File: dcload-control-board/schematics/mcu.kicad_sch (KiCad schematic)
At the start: 38 parts, among them J200 Conn_01x06_Male, J201 Conn_01x04_Male, J202 Conn_01x04_Male, U200 STM32F411RCT6, Y200 25MHz

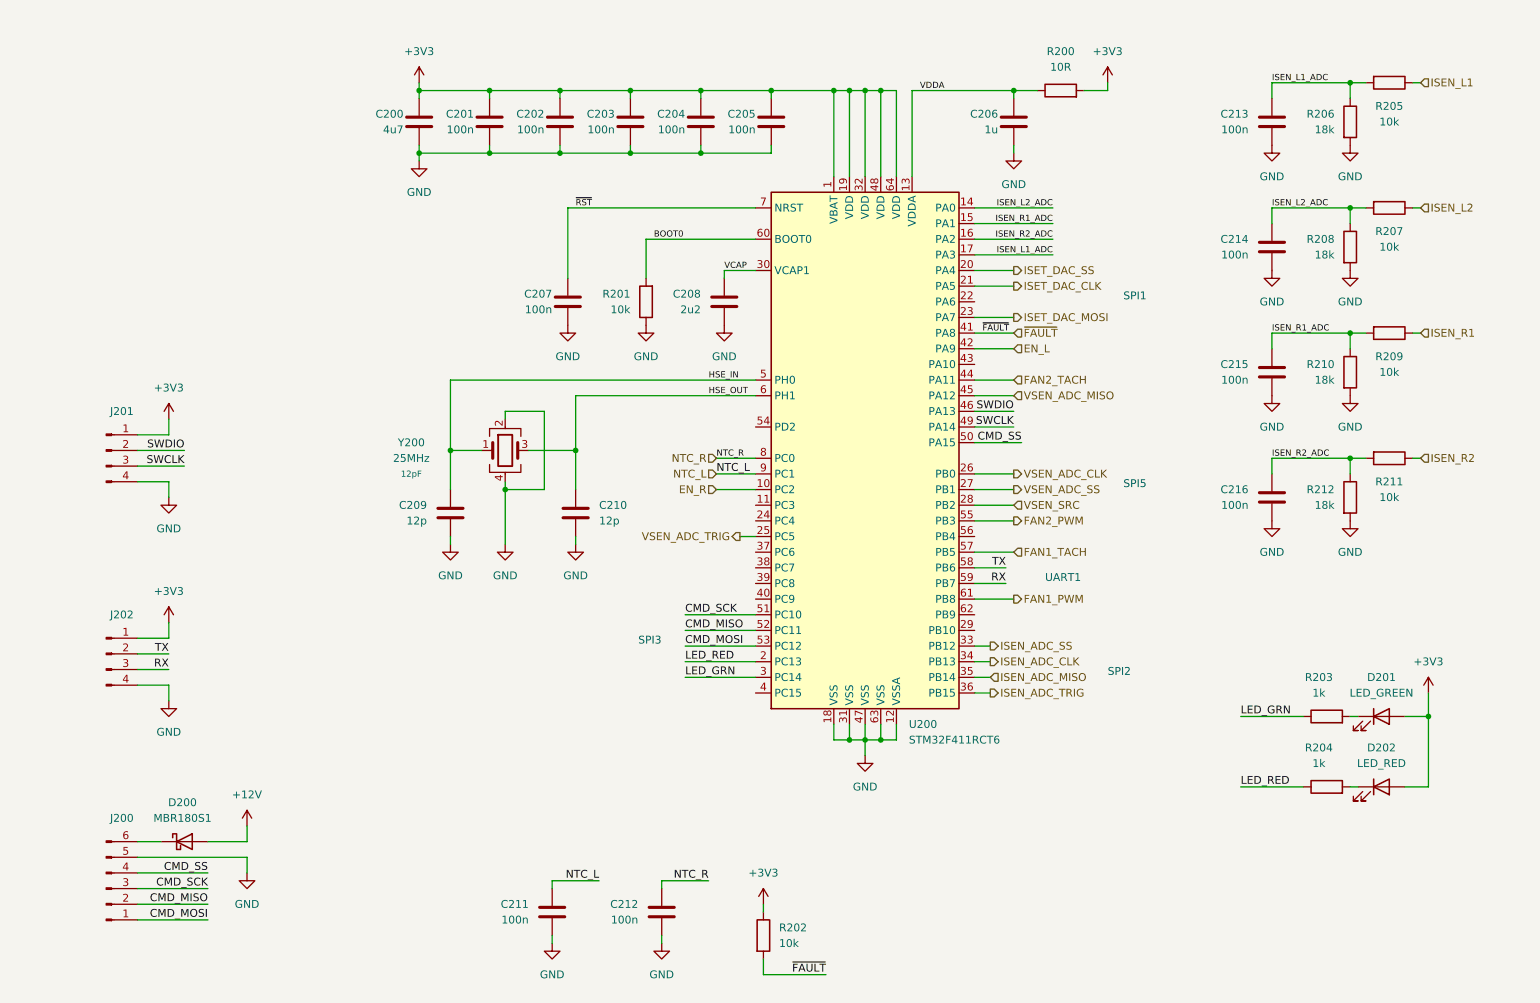
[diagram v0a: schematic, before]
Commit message: add: interface panel board
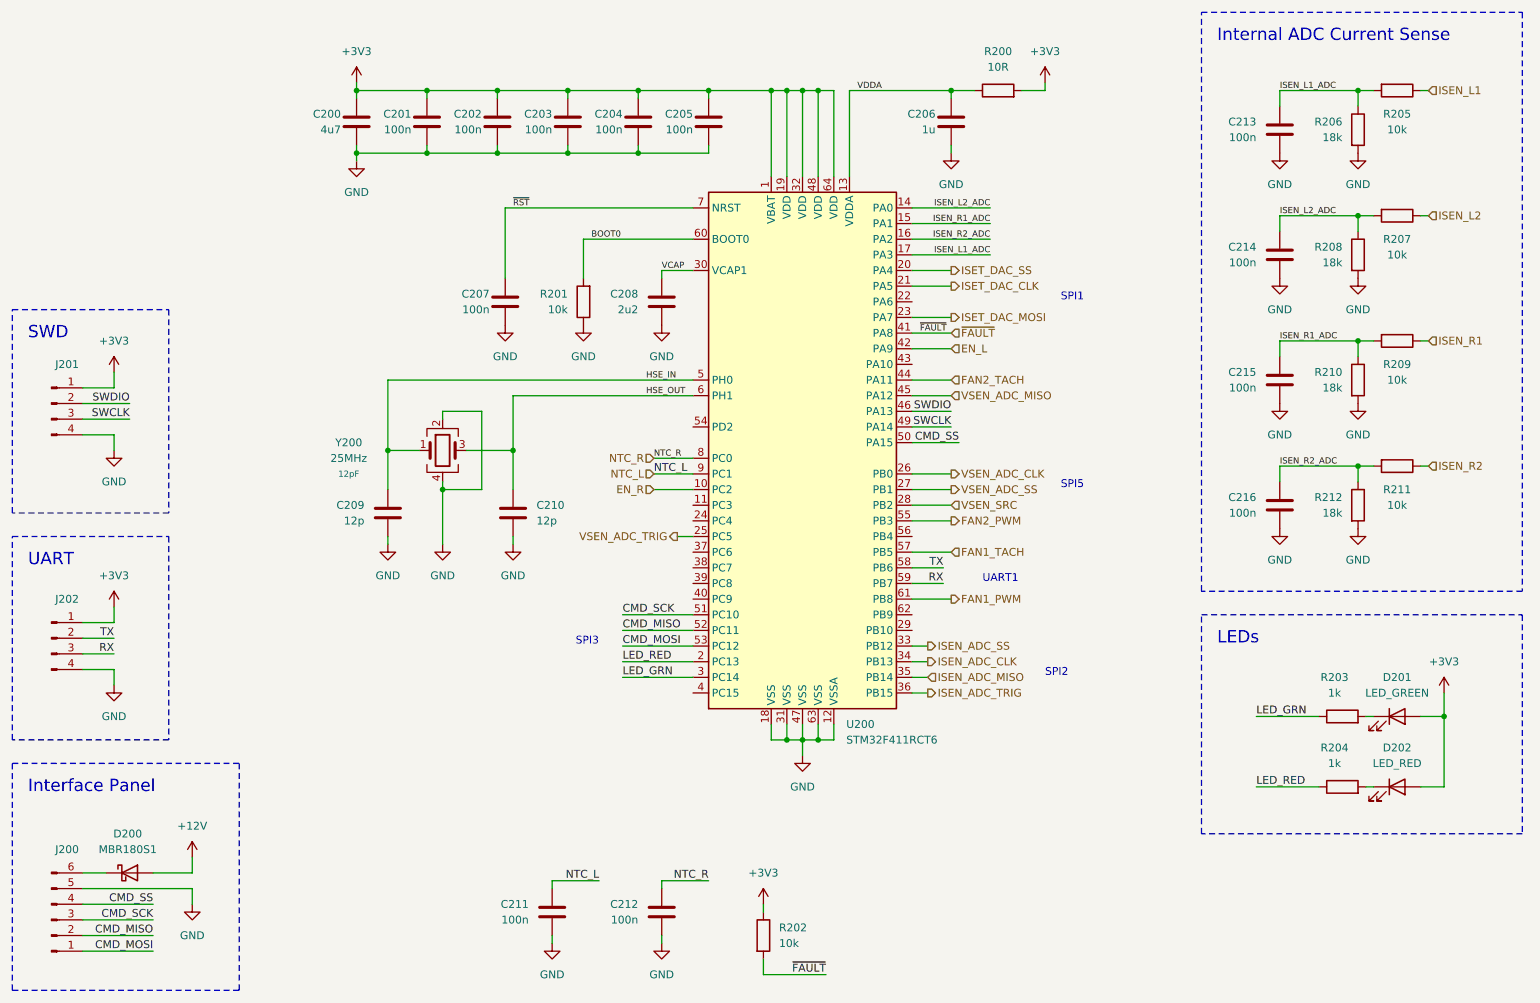
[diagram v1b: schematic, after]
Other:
- note added: "Interface Panel"
- note added: "Internal ADC Current Sense"
- note added: "LEDs"
- note added: "SWD"
- note added: "UART"
- moved on the sheet: C200, C201, C202, C203, C204, C205, C206, C207, C208, C209, C210, C213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
